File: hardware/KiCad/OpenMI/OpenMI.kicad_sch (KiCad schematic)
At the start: 0 parts

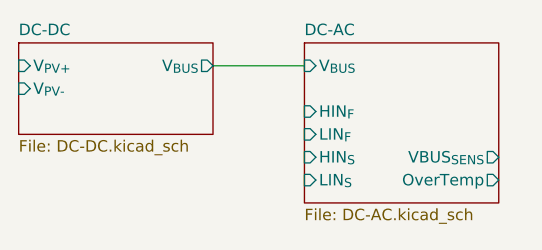
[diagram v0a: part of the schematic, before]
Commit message: fix(hw): update labels for GaNs of dc-dc converter
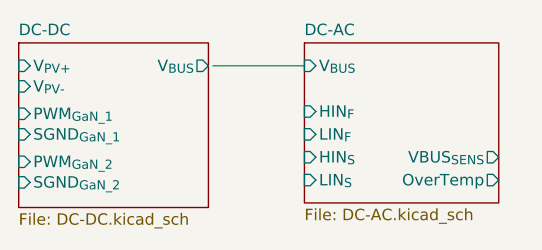
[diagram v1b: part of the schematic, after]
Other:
- sheet DC-DC ports: added PWM_{GaN_1}, PWM_{GaN_2}, SGND_{GaN_1}, SGND_{GaN_2}; removed none
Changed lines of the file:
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@@
     )
   )
-  (sheet (at 123.19 83.82) (size 21.59 10.16) (fields_autoplaced)
+  (sheet (at 123.19 83.82) (size 21.082 18.288) (fields_autoplaced)
     (stroke (width 0.1524) (type solid))
     (fill (color 0 0 0 0.0000))
@@
       (effects (font (size 1.27 1.27)) (justify left bottom))
     )
-    (property "Sheetfile" "DC-DC.kicad_sch" (at 123.19 94.5646 0)
+    (property "Sheetfile" "DC-DC.kicad_sch" (at 123.19 102.6926 0)
       (effects (font (size 1.27 1.27)) (justify left top))
     )
@@
       (effects (font (size 1.27 1.27)) (justify left))
     )
-    (pin "V_{PV-}" input (at 123.19 88.9 180)
+    (pin "V_{PV-}" input (at 123.19 88.646 180)
       (effects (font (size 1.27 1.27)) (justify left))
     )
-    (pin "V_{BUS}" output (at 144.78 86.36 0)
+    (pin "V_{BUS}" output (at 144.272 86.36 0)
       (effects (font (size 1.27 1.27)) (justify right))
     )
+    (pin "PWM_{GaN_1}" input (at 123.19 91.694 180)
+      (effects (font (size 1.27 1.27)) (justify left))
+    )
+    (pin "SGND_{GaN_1}" input (at 123.19 93.98 180)
+      (effects (font (size 1.27 1.27)) (justify left))
+    )
+    (pin "PWM_{GaN_2}" input (at 123.19 97.028 180)
+      (effects (font (size 1.27 1.27)) (justify left))
+    )
+    (pin "SGND_{GaN_2}" input (at 123.19 99.314 180)
+      (effects (font (size 1.27 1.27)) (justify left))
+    )
     (instances

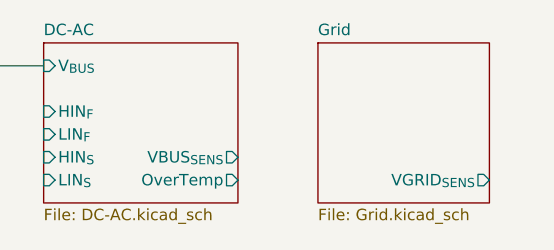
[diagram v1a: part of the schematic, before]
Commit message: feat: Add second grid voltage sens output.
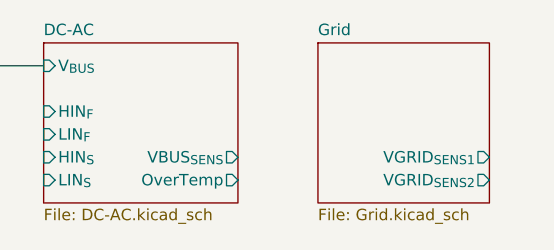
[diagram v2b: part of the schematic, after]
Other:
- sheet Grid ports: added VGRID_{SENS1}, VGRID_{SENS2}; removed VGRID_{SENS}
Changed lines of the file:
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@@
       (effects (font (size 1.27 1.27)) hide)
     )
-    (pin "VGRID_{SENS}" output (at 204.47 99.06 0)
+    (pin "VGRID_{SENS2}" output (at 204.47 99.06 0)
       (effects (font (size 1.27 1.27)) (justify right))
     )
+    (pin "VGRID_{SENS1}" output (at 204.47 96.52 0)
+      (effects (font (size 1.27 1.27)) (justify right))
+    )

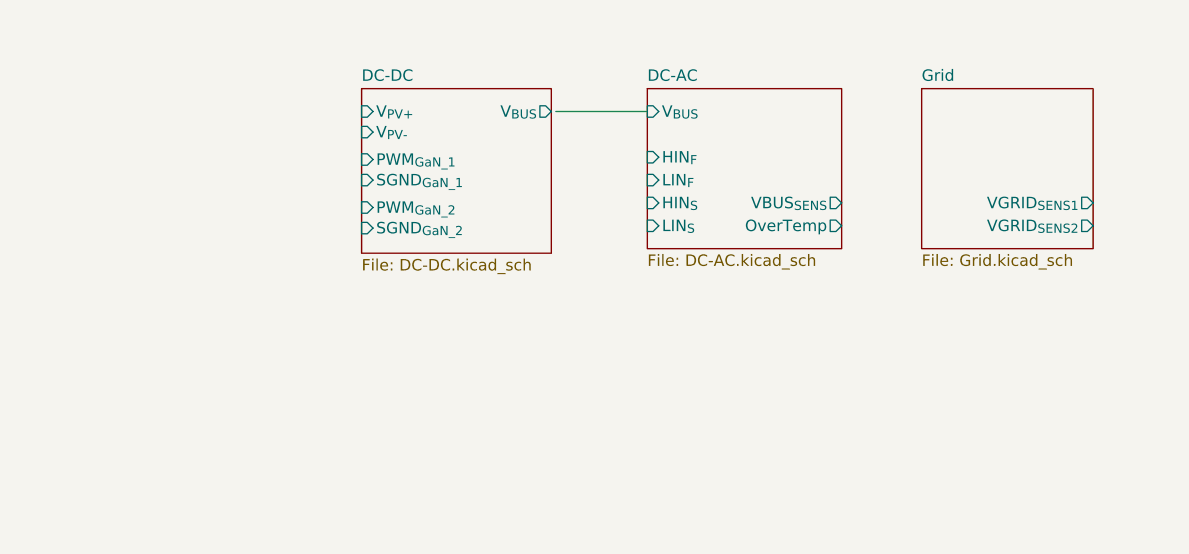
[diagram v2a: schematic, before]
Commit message: feat(hw): Adds inverter current sensing
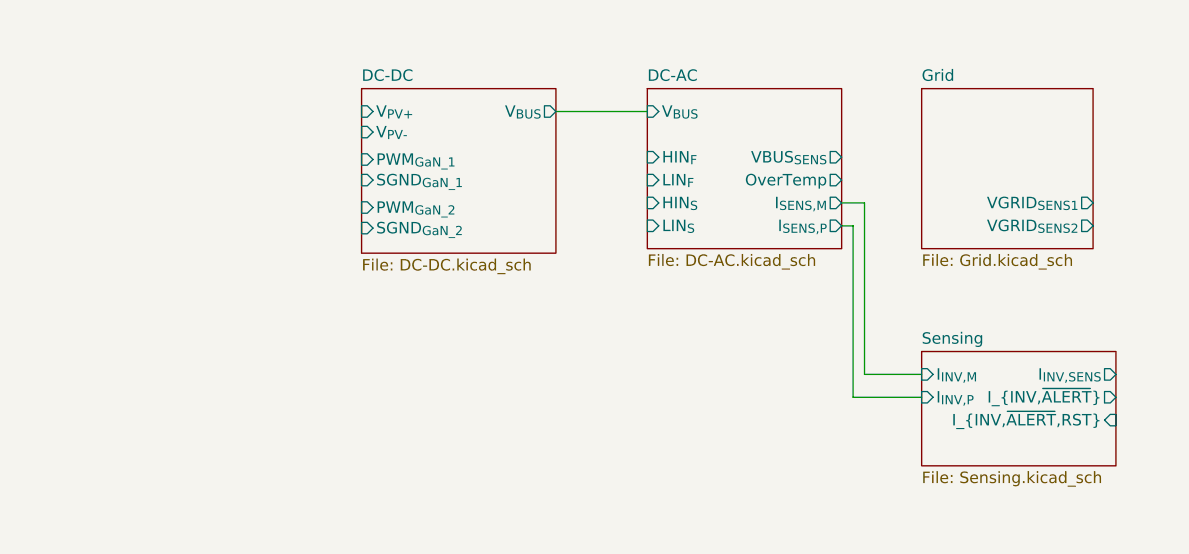
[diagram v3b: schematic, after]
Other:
- added sheet Sensing (Sensing.kicad_sch)
- sheet DC-AC ports: added I_{SENS,M}, I_{SENS,P}; removed none
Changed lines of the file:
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@@
 (kicad_sch (version 20230121) (generator eeschema)
   (paper "A4")
+  (wire (pts (xy 176.53 96.52) (xy 179.07 96.52))
+    (stroke (width 0) (type default))
+  )
+  (wire (pts (xy 176.53 99.06) (xy 177.8 99.06))
+    (stroke (width 0) (type default))
+  )
+  (wire (pts (xy 179.07 96.52) (xy 179.07 115.57))
+    (stroke (width 0) (type default))
+  )
   (wire (pts (xy 144.78 86.36) (xy 154.94 86.36))
+    (stroke (width 0) (type default))
+  )
+  (wire (pts (xy 177.8 99.06) (xy 177.8 118.11))
+    (stroke (width 0) (type default))
+  )
+  (wire (pts (xy 179.07 115.57) (xy 185.42 115.57))
+    (stroke (width 0) (type default))
+  )
+  (wire (pts (xy 177.8 118.11) (xy 185.42 118.11))
     (stroke (width 0) (type default))
   )
@@
       (effects (font (size 1.27 1.27)) (justify left))
     )
-    (pin "OverTemp" output (at 176.53 99.06 0)
+    (pin "OverTemp" output (at 176.53 93.98 0)
       (effects (font (size 1.27 1.27)) (justify right))
     )
@@
       (effects (font (size 1.27 1.27)) (justify left))
     )
-    (pin "VBUS_{SENS}" output (at 176.53 96.52 0)
+    (pin "VBUS_{SENS}" output (at 176.53 91.44 0)
+      (effects (font (size 1.27 1.27)) (justify right))
+    )
+    (pin "I_{SENS,M}" output (at 176.53 96.52 0)
+      (effects (font (size 1.27 1.27)) (justify right))
+    )
+    (pin "I_{SENS,P}" output (at 176.53 99.06 0)
       (effects (font (size 1.27 1.27)) (justify right))
     )
@@
     )
   )
-  (sheet (at 123.19 83.82) (size 21.082 18.288) (fields_autoplaced)
+  (sheet (at 185.42 113.03) (size 21.59 12.7) (fields_autoplaced)
+    (stroke (width 0.1524) (type solid))
+    (fill (color 0 0 0 0.0000))
+    (property "Sheetname" "Sensing" (at 185.42 112.3184 0)
+      (effects (font (size 1.27 1.27)) (justify left bottom))
+    )
+    (property "Sheetfile" "Sensing.kicad_sch" (at 185.42 126.3146 0)
+      (effects (font (size 1.27 1.27)) (justify left top))
+    )
+    (pin "I_{INV,M}" input (at 185.42 115.57 180)
+      (effects (font (size 1.27 1.27)) (justify left))
+    )
+    (pin "I_{INV,P}" input (at 185.42 118.11 180)
+      (effects (font (size 1.27 1.27)) (justify left))
+    )
+    (pin "I_{INV,~{ALERT}}" output (at 207.01 118.11 0)
+      (effects (font (size 1.27 1.27)) (justify right))
+    )
+    (pin "I_{INV,~{ALERT},RST}" input (at 207.01 120.65 0)
+      (effects (font (size 1.27 1.27)) (justify right))
+    )
+    (pin "I_{INV,SENS}" output (at 207.01 115.57 0)
+      (effects (font (size 1.27 1.27)) (justify right))
+    )
+    (instances
+      (project "OpenMI"
+        (path "/2d959e19-1572-42a0-a8fd-da8463ad4e66" (page "5"))
+      )
+    )
+  )
+  (sheet (at 123.19 83.82) (size 21.59 18.288) (fields_autoplaced)
     (stroke (width 0.1524) (type solid))
     (fill (color 0 0 0 0.0000))
@@
       (effects (font (size 1.27 1.27)) (justify left))
     )
-    (pin "V_{BUS}" output (at 144.272 86.36 0)
+    (pin "V_{BUS}" output (at 144.78 86.36 0)
       (effects (font (size 1.27 1.27)) (justify right))
     )

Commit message: feat(hw): Moves DC-bus sense to Sensing sheet. Adds op-amp for impedance decoupling.
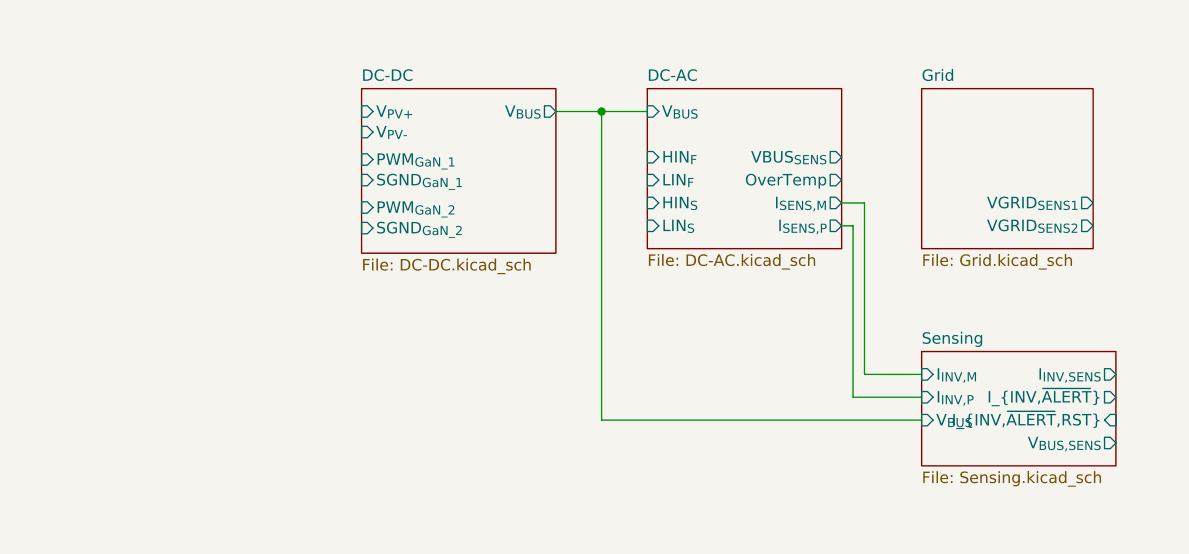
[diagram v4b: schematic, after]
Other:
- sheet Sensing ports: added V_{BUS,SENS}, V_{BUS}; removed none
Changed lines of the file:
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@@
 (kicad_sch (version 20230121) (generator eeschema)
   (paper "A4")
+  (junction (at 149.86 86.36) (diameter 0) (color 0 0 0 0)
+  )
+  (wire (pts (xy 149.86 86.36) (xy 154.94 86.36))
+    (stroke (width 0) (type default))
+  )
+  (wire (pts (xy 149.86 86.36) (xy 149.86 120.65))
+    (stroke (width 0) (type default))
+  )
   (wire (pts (xy 176.53 96.52) (xy 179.07 96.52))
     (stroke (width 0) (type default))
@@
     (stroke (width 0) (type default))
   )
-  (wire (pts (xy 144.78 86.36) (xy 154.94 86.36))
+  (wire (pts (xy 144.78 86.36) (xy 149.86 86.36))
     (stroke (width 0) (type default))
   )
@@
   )
   (wire (pts (xy 177.8 118.11) (xy 185.42 118.11))
+    (stroke (width 0) (type default))
+  )
+  (wire (pts (xy 149.86 120.65) (xy 185.42 120.65))
     (stroke (width 0) (type default))
   )
@@
       (effects (font (size 1.27 1.27)) (justify right))
     )
+    (pin "V_{BUS}" input (at 185.42 120.65 180)
+      (effects (font (size 1.27 1.27)) (justify left))
+    )
+    (pin "V_{BUS,SENS}" output (at 207.01 123.19 0)
+      (effects (font (size 1.27 1.27)) (justify right))
+    )

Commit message: refactor(hw): Moves grid voltage sensing to `Sensing`. Refactors labels.
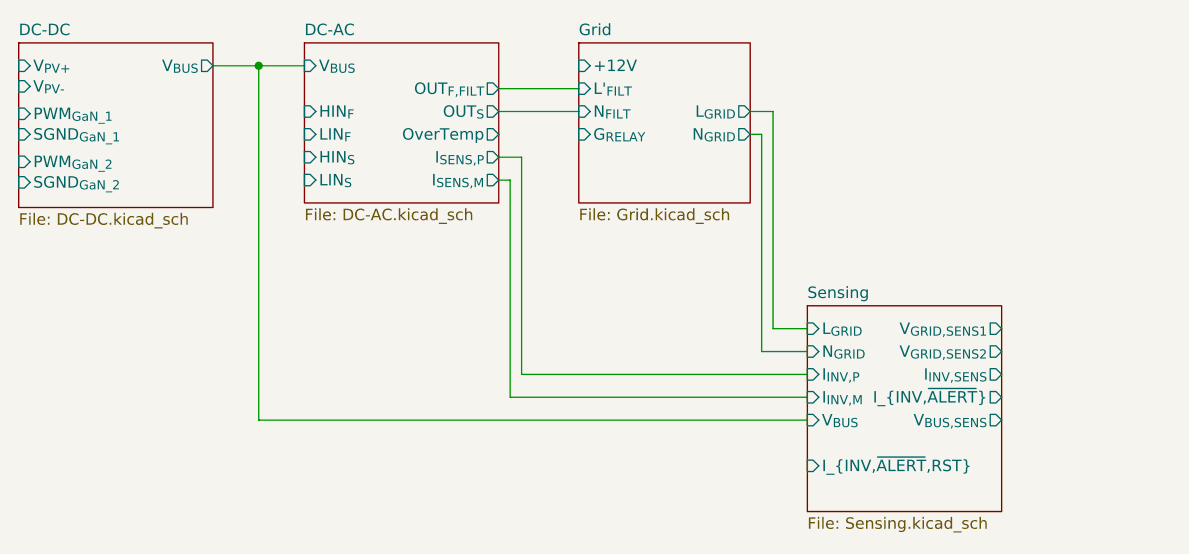
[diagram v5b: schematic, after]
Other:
- sheet DC-AC ports: added OUT_{F,FILT}, OUT_{S}; removed VBUS_{SENS}
- sheet Grid ports: added +12V, G_{RELAY}, L'_{FILT}, L_{GRID}, N_{FILT}, N_{GRID}; removed VGRID_{SENS1}, VGRID_{SENS2}
- sheet Sensing ports: added L_{GRID}, N_{GRID}, V_{GRID,SENS1}, V_{GRID,SENS2}; removed none

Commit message: feat: Adds grid current sensing using a hall effect sensor.
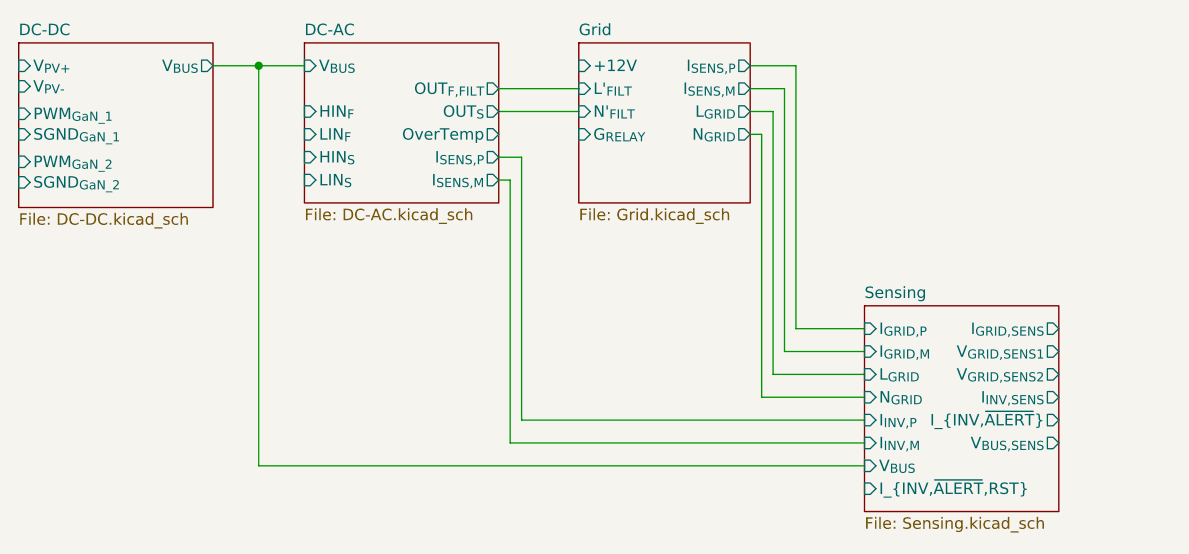
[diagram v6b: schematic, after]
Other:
- sheet Grid ports: added I_{SENS,M}, I_{SENS,P}, N'_{FILT}; removed N_{FILT}
- sheet Sensing ports: added I_{GRID,M}, I_{GRID,P}, I_{GRID,SENS}; removed none
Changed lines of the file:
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@@
     (stroke (width 0) (type default))
   )
-  (wire (pts (xy 111.76 81.28) (xy 111.76 120.65))
+  (wire (pts (xy 111.76 81.28) (xy 111.76 125.73))
     (stroke (width 0) (type default))
   )
@@
     (stroke (width 0) (type default))
   )
-  (wire (pts (xy 140.97 91.44) (xy 140.97 115.57))
+  (wire (pts (xy 140.97 91.44) (xy 140.97 120.65))
     (stroke (width 0) (type default))
   )
@@
     (stroke (width 0) (type default))
   )
-  (wire (pts (xy 139.7 93.98) (xy 139.7 118.11))
-    (stroke (width 0) (type default))
-  )
-  (wire (pts (xy 140.97 115.57) (xy 172.72 115.57))
+  (wire (pts (xy 139.7 93.98) (xy 139.7 123.19))
+    (stroke (width 0) (type default))
+  )
+  (wire (pts (xy 140.97 120.65) (xy 179.07 120.65))
+    (stroke (width 0) (type default))
+  )
+  (wire (pts (xy 170.18 113.03) (xy 179.07 113.03))
     (stroke (width 0) (type default))
   )
@@
     (stroke (width 0) (type default))
   )
-  (wire (pts (xy 167.64 88.9) (xy 167.64 113.03))
-    (stroke (width 0) (type default))
-  )
-  (wire (pts (xy 139.7 118.11) (xy 172.72 118.11))
+  (wire (pts (xy 166.37 83.82) (xy 170.18 83.82))
+    (stroke (width 0) (type default))
+  )
+  (wire (pts (xy 170.18 83.82) (xy 170.18 113.03))
+    (stroke (width 0) (type default))
+  )
+  (wire (pts (xy 167.64 88.9) (xy 167.64 118.11))
+    (stroke (width 0) (type default))
+  )
+  (wire (pts (xy 139.7 123.19) (xy 179.07 123.19))
     (stroke (width 0) (type default))
   )
@@
     (stroke (width 0) (type default))
   )
-  (wire (pts (xy 172.72 113.03) (xy 167.64 113.03))
-    (stroke (width 0) (type default))
-  )
-  (wire (pts (xy 168.91 110.49) (xy 172.72 110.49))
-    (stroke (width 0) (type default))
-  )
-  (wire (pts (xy 111.76 120.65) (xy 172.72 120.65))
-    (stroke (width 0) (type default))
-  )
-  (wire (pts (xy 168.91 86.36) (xy 168.91 110.49))
+  (wire (pts (xy 179.07 118.11) (xy 167.64 118.11))
+    (stroke (width 0) (type default))
+  )
+  (wire (pts (xy 171.45 110.49) (xy 171.45 81.28))
+    (stroke (width 0) (type default))
+  )
+  (wire (pts (xy 168.91 115.57) (xy 179.07 115.57))
+    (stroke (width 0) (type default))
+  )
+  (wire (pts (xy 111.76 125.73) (xy 179.07 125.73))
+    (stroke (width 0) (type default))
+  )
+  (wire (pts (xy 168.91 86.36) (xy 168.91 115.57))
+    (stroke (width 0) (type default))
+  )
+  (wire (pts (xy 179.07 110.49) (xy 171.45 110.49))
+    (stroke (width 0) (type default))
+  )
+  (wire (pts (xy 171.45 81.28) (xy 166.37 81.28))
     (stroke (width 0) (type default))
   )
@@
       (effects (font (size 1.27 1.27)) (justify left))
     )
-    (pin "N_{FILT}" input (at 147.32 86.36 180)
-      (effects (font (size 1.27 1.27)) (justify left))
-    )
     (pin "G_{RELAY}" input (at 147.32 88.9 180)
       (effects (font (size 1.27 1.27)) (justify left))
     )
     (pin "L'_{FILT}" input (at 147.32 83.82 180)
+      (effects (font (size 1.27 1.27)) (justify left))
+    )
+    (pin "I_{SENS,P}" output (at 166.37 81.28 0)
+      (effects (font (size 1.27 1.27)) (justify right))
+    )
+    (pin "I_{SENS,M}" output (at 166.37 83.82 0)
+      (effects (font (size 1.27 1.27)) (justify right))
+    )
+    (pin "N'_{FILT}" input (at 147.32 86.36 180)
       (effects (font (size 1.27 1.27)) (justify left))
     )
@@
     )
   )
-  (sheet (at 172.72 107.95) (size 21.59 22.86) (fields_autoplaced)
+  (sheet (at 179.07 107.95) (size 21.59 22.86) (fields_autoplaced)
     (stroke (width 0.1524) (type solid))
     (fill (color 0 0 0 0.0000))
-    (property "Sheetname" "Sensing" (at 172.72 107.2384 0)
+    (property "Sheetname" "Sensing" (at 179.07 107.2384 0)
       (effects (font (size 1.27 1.27)) (justify left bottom))
     )
-    (property "Sheetfile" "Sensing.kicad_sch" (at 172.72 131.3946 0)
+    (property "Sheetfile" "Sensing.kicad_sch" (at 179.07 131.3946 0)
       (effects (font (size 1.27 1.27)) (justify left top))
     )
-    (pin "I_{INV,M}" input (at 172.72 118.11 180)
-      (effects (font (size 1.27 1.27)) (justify left))
-    )
-    (pin "I_{INV,P}" input (at 172.72 115.57 180)
-      (effects (font (size 1.27 1.27)) (justify left))
-    )
-    (pin "I_{INV,~{ALERT}}" output (at 194.31 118.11 0)
-      (effects (font (size 1.27 1.27)) (justify right))
-    )
-    (pin "I_{INV,~{ALERT},RST}" input (at 172.72 125.73 180)
-      (effects (font (size 1.27 1.27)) (justify left))
-    )
-    (pin "I_{INV,SENS}" output (at 194.31 115.57 0)
-      (effects (font (size 1.27 1.27)) (justify right))
-    )
-    (pin "V_{BUS}" input (at 172.72 120.65 180)
-      (effects (font (size 1.27 1.27)) (justify left))
-    )
-    (pin "V_{BUS,SENS}" output (at 194.31 120.65 0)
-      (effects (font (size 1.27 1.27)) (justify right))
-    )
-    (pin "L_{GRID}" input (at 172.72 110.49 180)
-      (effects (font (size 1.27 1.27)) (justify left))
-    )
-    (pin "N_{GRID}" input (at 172.72 113.03 180)
-      (effects (font (size 1.27 1.27)) (justify left))
-    )
-    (pin "V_{GRID,SENS1}" output (at 194.31 110.49 0)
-      (effects (font (size 1.27 1.27)) (justify right))
-    )
-    (pin "V_{GRID,SENS2}" output (at 194.31 113.03 0)
-      (effects (font (size 1.27 1.27)) (justify right))
+    (pin "I_{INV,M}" input (at 179.07 123.19 180)
+      (effects (font (size 1.27 1.27)) (justify left))
+    )
+    (pin "I_{INV,P}" input (at 179.07 120.65 180)
+      (effects (font (size 1.27 1.27)) (justify left))
+    )
+    (pin "I_{INV,~{ALERT}}" output (at 200.66 120.65 0)
+      (effects (font (size 1.27 1.27)) (justify right))
+    )
+    (pin "I_{INV,~{ALERT},RST}" input (at 179.07 128.27 180)
+      (effects (font (size 1.27 1.27)) (justify left))
+    )
+    (pin "I_{INV,SENS}" output (at 200.66 118.11 0)
+      (effects (font (size 1.27 1.27)) (justify right))
+    )
+    (pin "V_{BUS}" input (at 179.07 125.73 180)
+      (effects (font (size 1.27 1.27)) (justify left))
+    )
+    (pin "V_{BUS,SENS}" output (at 200.66 123.19 0)
+      (effects (font (size 1.27 1.27)) (justify right))
+    )
+    (pin "L_{GRID}" input (at 179.07 115.57 180)
+      (effects (font (size 1.27 1.27)) (justify left))
+    )
+    (pin "N_{GRID}" input (at 179.07 118.11 180)
+      (effects (font (size 1.27 1.27)) (justify left))
+    )
+    (pin "V_{GRID,SENS1}" output (at 200.66 113.03 0)
+      (effects (font (size 1.27 1.27)) (justify right))
+    )
+    (pin "V_{GRID,SENS2}" output (at 200.66 115.57 0)
+      (effects (font (size 1.27 1.27)) (justify right))
+    )
+    (pin "I_{GRID,SENS}" output (at 200.66 110.49 0)
+      (effects (font (size 1.27 1.27)) (justify right))
+    )
+    (pin "I_{GRID,P}" input (at 179.07 110.49 180)
+      (effects (font (size 1.27 1.27)) (justify left))
+    )
+    (pin "I_{GRID,M}" input (at 179.07 113.03 180)
+      (effects (font (size 1.27 1.27)) (justify left))
     )
     (instances
